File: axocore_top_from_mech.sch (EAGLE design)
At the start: 13 parts, among them U1 JOYSTICKPTH, X1 X1, X3 M02PTH, X4 M02PTH

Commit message: finalised layout, starting routing
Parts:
- removed S1: SWITCH-MOMENTARY-212MM, SparkFun-Electromechanical:SWITCH-MOMENTARY-212MM
- removed VR1, VR2, VR3, VR4, VR5, VR6: (no value), MusicThingModular:9MM_SNAP-IN_POT_
- added BIG_S3: SWITCH-MOMENTARY-212MM, SparkFun-Electromechanical:SWITCH-MOMENTARY-212MM
- added LED1, LED2, LED3, LED4: (no value), SparkFun-LED:LED3MM
- added POT_PA2, POT_PA3, POT_PA4, POT_PA5, POT_PA6, POT_PA7, VR7: (no value), MusicThingModular:9MM_SNAP-IN_POT_
- added R1, R2, R3, R4: (no value), MusicThingModular:RESISTOR7MM
- added SMALL_S1, SMALL_S2, SMALL_S3: SWITCH-MOMENTARY-2PTH, SparkFun-Electromechanical:SWITCH-MOMENTARY-2PTH
- renumbered S2 to BIG_S2, S3 to BIG_S1
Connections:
- new net CM: X1.31
- new net G: X1.32, X1.33
- new net GND: POT_PA2.A, POT_PA3.A, POT_PA4.A, POT_PA5.A, POT_PA6.A, POT_PA7.A, U1.H-, U1.V-, VR7.A, X1.14, X1.20, X1.28, X1.40, X1.6
- new net LIN+: X1.34
- new net LIN-: X1.35
- new net N$1: BIG_S3.1, SMALL_S3.1
- new net N$10: LED4.C, R4.1
- new net N$2: BIG_S3.2, SMALL_S3.2
- new net N$3: BIG_S2.1, SMALL_S2.1
- new net N$4: BIG_S2.2, SMALL_S2.2
- new net N$5: BIG_S1.1, SMALL_S1.1
- new net N$6: BIG_S1.2, SMALL_S1.2
- new net N$7: LED1.C, R1.2
- new net N$8: LED2.C, R2.2
- new net N$9: LED3.C, R3.2
- new net PA0: U1.H, X1.16
- new net PA1: U1.V, VR7.S, X1.17
- new net PA2: POT_PA2.S, X1.18
- new net PA3: POT_PA3.S, X1.19
- new net PA4: POT_PA4.S, X1.22
- new net PA5: POT_PA5.S, X1.23
- new net PA6: POT_PA6.S, X1.24
- new net PA7: POT_PA7.S, X1.25
- new net PB0: X1.26
- new net PB1: X1.27
- new net PB6: X1.2
- new net PB7: X1.3
- new net PB8: X1.4
- new net PB9: X1.5
- new net PC0: X1.8
- new net PC1: X1.9
- new net PC2: X1.10
- new net PC3: X1.11
- new net PC4: X1.12
- new net PC5: X1.13
- new net RIN+: X1.36
- new net RIN-: X1.37
- new net VDD: X1.1, X1.7
- new net VDDA: POT_PA2.E, POT_PA3.E, POT_PA4.E, POT_PA5.E, POT_PA6.E, POT_PA7.E, U1.H+, U1.V+, VR7.E, X1.15, X1.21
- new net VDDC: X1.29, X1.30
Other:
- note added: "ANALOG: 8 POTs / analog in PB1 PB0 PA7 PA6 PA5 PA4 PA0 PA1 DIGITAL 4 Digi Ins for switches PA2 PA3 PC5 PC4 4 PWM outputs for LEDs CHECK PC3 PC1 PC0 PB9 PB8 PB7 PB6"
- note added: "Parts: PS3 thumb joystick Pots: 5-50k Linear D Shaft Bourns PTV09A-4020F-B103 Alps RK09K11310KB B3F-4050 = 12mm square tactile switches B32-1310 = black keycap B32-1320 = orange B32-1330 = yellow B32-1360 = white B32-1380 = red 11mm spacer bolts"
- moved on the sheet: U1

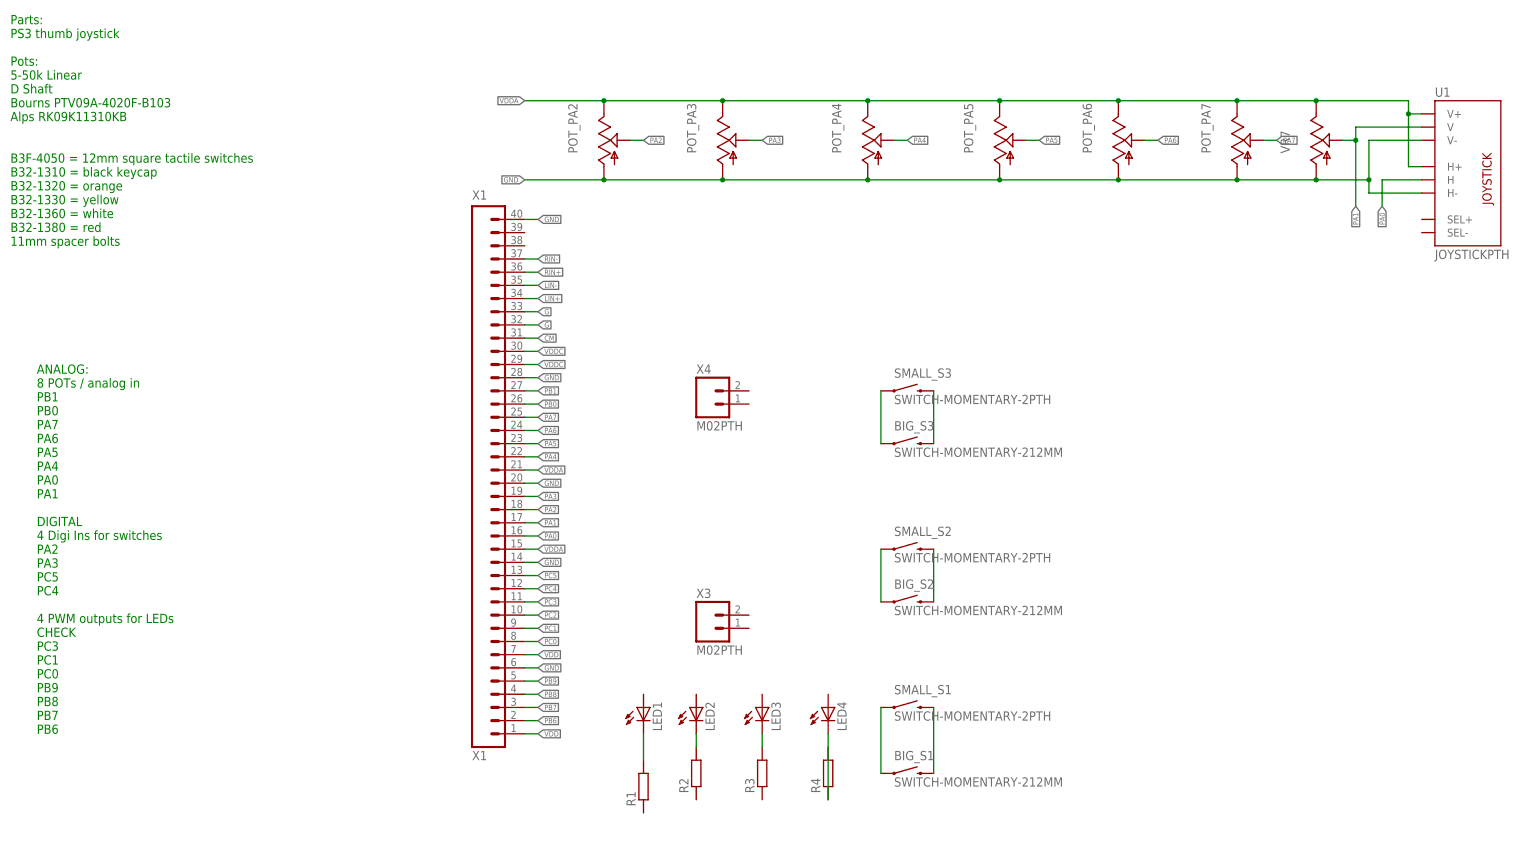
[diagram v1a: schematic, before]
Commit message: Completed routing
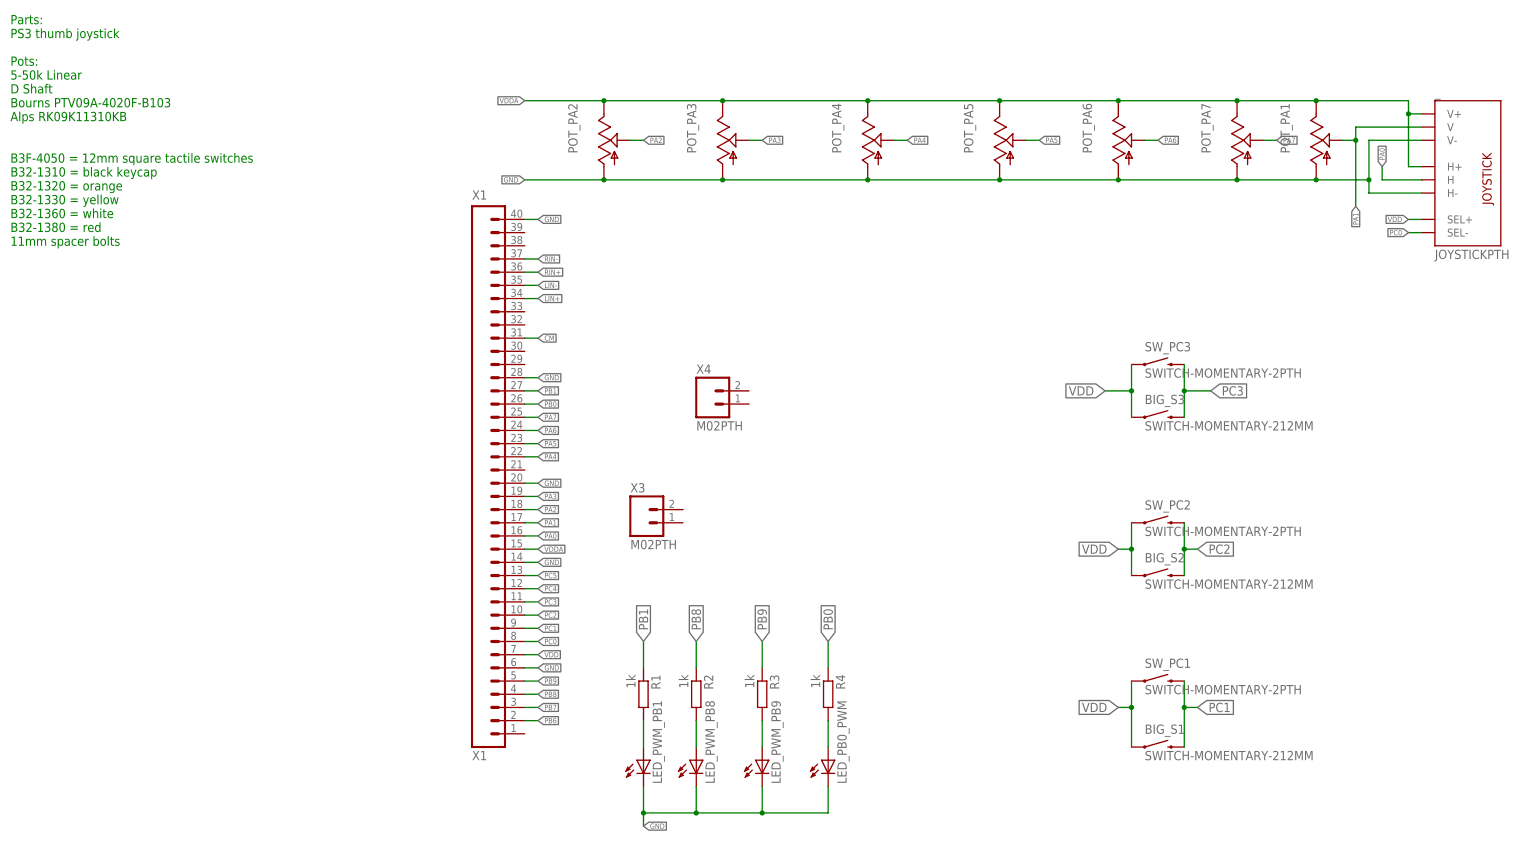
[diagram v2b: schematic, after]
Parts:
- removed LED1, LED2, LED3, LED4: (no value), SparkFun-LED:LED3MM
- removed SMALL_S1, SMALL_S2, SMALL_S3: SWITCH-MOMENTARY-2PTH, SparkFun-Electromechanical:SWITCH-MOMENTARY-2PTH
- added LED_PB0_PWM, LED_PWM_PB1, LED_PWM_PB8, LED_PWM_PB9: (no value), SparkFun-LED:LED3MM
- added SW_PC1, SW_PC2, SW_PC3: SWITCH-MOMENTARY-2PTH, SparkFun-Electromechanical:SWITCH-MOMENTARY-2PTH
- R1, R2, R3, R4: value (none) -> 1k
- renumbered U1 to _, VR7 to POT_PA1
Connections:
- removed net G: X1.32, X1.33
- removed net N$1: BIG_S3.1, SMALL_S3.1
- removed net N$2: BIG_S3.2, SMALL_S3.2
- removed net N$3: BIG_S2.1, SMALL_S2.1
- removed net N$4: BIG_S2.2, SMALL_S2.2
- removed net N$5: BIG_S1.1, SMALL_S1.1
- removed net N$6: BIG_S1.2, SMALL_S1.2
- removed net VDDC: X1.29, X1.30
- net GND: now also LED_PB0_PWM.C, LED_PWM_PB1.C, LED_PWM_PB8.C, LED_PWM_PB9.C
- net N$10: now also LED_PB0_PWM.A, R4.2; no longer LED4.C, R4.1
- net N$7: now also LED_PWM_PB1.A; no longer LED1.C
- net N$8: now also LED_PWM_PB8.A; no longer LED2.C
- net N$9: now also LED_PWM_PB9.A; no longer LED3.C
- net PB0: now also R4.1
- net PB1: now also R1.1
- net PB8: now also R2.1
- net PB9: now also R3.1
- net PC0: now also _.SEL-
- net PC1: now also BIG_S1.2, SW_PC1.2
- net PC2: now also BIG_S2.2, SW_PC2.2
- net PC3: now also BIG_S3.2, SW_PC3.2
- net VDD: now also BIG_S1.1, BIG_S2.1, BIG_S3.1, SW_PC1.1, SW_PC2.1, SW_PC3.1, _.SEL+; no longer X1.1
- net VDDA: no longer X1.21
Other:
- note removed: "ANALOG: 8 POTs / analog in PB1 PB0 PA7 PA6 PA5 PA4 PA0 PA1 DIGITAL 4 Digi Ins for switches PA2 PA3 PC5 PC4 4 PWM outputs for LEDs CHECK PC3 PC1 PC0 PB9 PB8 PB7 PB6"
- moved on the sheet: BIG_S1, BIG_S2, BIG_S3, R1, R2, R3, R4, X3

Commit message: Rev 1 Complete and sent to OSHPark
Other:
- note added: "Parts: PS3 thumb joystick 6 x 10k Linear D Shaft Pots Bourns PTV09A-4020F-B103 Alps RK09K11310KB 3 x 12mm square tactile switches B3F-4050 = switch B32-1310 = black keycap B32-1320 = orange B32-1330 = yellow B32-1360 = white B32-1380 = red 4 x 1k Resistors 4 x 3mm LEDs 4 x 11mm M3 Hex Standoffs 2 x 2 pin Female Header 571-215297-2 40 pin Female Header"
- note removed: "Parts: PS3 thumb joystick Pots: 5-50k Linear D Shaft Bourns PTV09A-4020F-B103 Alps RK09K11310KB B3F-4050 = 12mm square tactile switches B32-1310 = black keycap B32-1320 = orange B32-1330 = yellow B32-1360 = white B32-1380 = red 11mm spacer bolts"
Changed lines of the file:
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@@
 <sheet>
 <plain>
-<text x="-35.56" y="96.52" size="1.778" layer="91">Parts:
+<text x="-35.56" y="96.52" size="1.016" layer="91">Parts:
 PS3 thumb joystick
-Pots:
-5-50k Linear
-D Shaft
+6 x 10k Linear D Shaft Pots
 Bourns PTV09A-4020F-B103
 Alps RK09K11310KB
-B3F-4050 = 12mm square tactile switches
+3 x 12mm square tactile switches
+B3F-4050 = switch
 B32-1310 = black keycap
 B32-1320 = orange
@@
 B32-1360 = white
 B32-1380 = red
-11mm spacer bolts </text>
+4 x 1k Resistors
+4 x 3mm LEDs
+4 x 11mm M3 Hex Standoffs
+2 x 2 pin Female Header 571-215297-2
+40 pin Female Header</text>
 </plain>
 <instances>
